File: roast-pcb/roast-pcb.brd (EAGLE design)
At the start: 3 parts

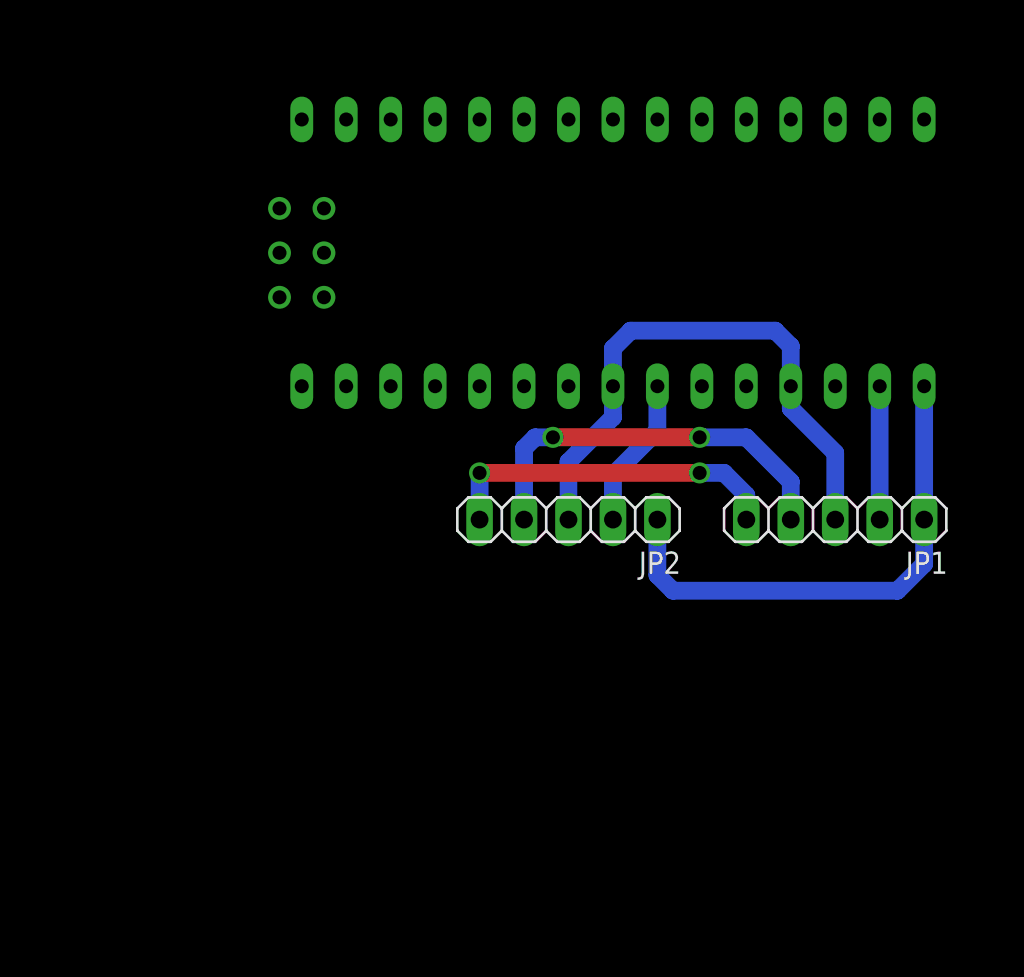
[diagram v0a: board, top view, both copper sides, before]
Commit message: ready to print PCB design
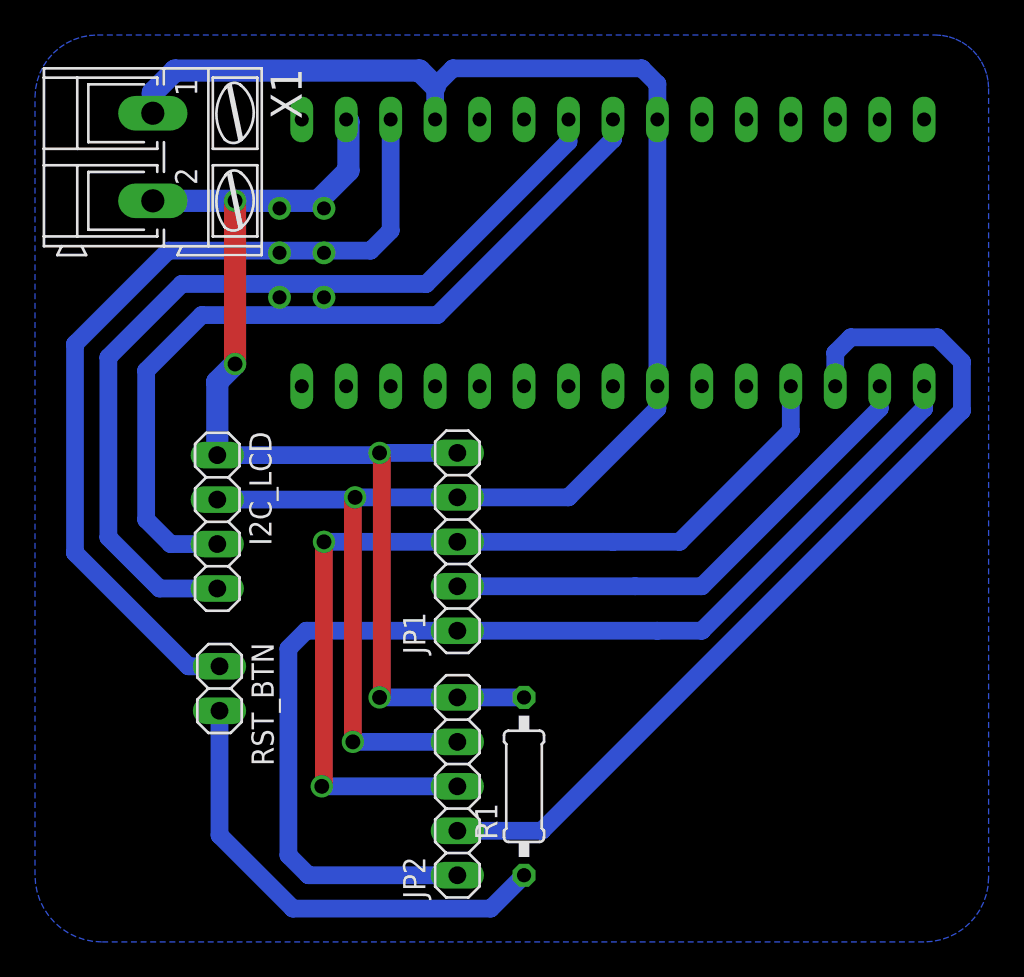
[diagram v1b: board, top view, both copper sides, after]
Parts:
- added I2C_LCD: (no value), pinhead:1X04
- added R1: (no value), rcl:0207/10
- added RST_BTN: (no value), pinhead:1X02
- added X1: (no value), con-ptr500:AK300/2
- moved JP1 21.6 mm to (38.1, 19.1), turned to 90 degrees
- moved JP2 16.5 mm to (38.1, 5.08), turned to 90 degrees
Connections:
- new net CS2: JP2.2, U$1.D10
- new net N$5: R1.1, RST_BTN.2
- new net SCL: I2C_LCD.4, U$1.A5
- new net SDA: I2C_LCD.3, U$1.A4
- net +5V: now also I2C_LCD.2, U$1.5V, X1.1
- net GND: now also I2C_LCD.1, R1.2, U$1.GND, X1.2
- net N$1: now also RST_BTN.1, U$1.RST; no longer JP2.2, U$1.D6
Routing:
- net +5V: track 22.8 -> 99.4 mm, vias 2 -> 4
- net CS2: track 0.00 -> 51.7 mm
- net SCL: track 0.00 -> 50.4 mm
- net SDA: track 0.00 -> 46.4 mm
- net GND: track 19.8 -> 65.7 mm, vias 2 -> 4
- net N$1: track 8.67 -> 49.9 mm
- net SO: track 29.6 -> 65.2 mm
- net N$5: track 0.00 -> 27.0 mm
- net CS1: track 7.62 -> 29.6 mm
- net SCK: track 32.7 -> 53.6 mm, vias 0 -> 4
- added copper zone on layer 16, net GND

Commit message: test ready sensor
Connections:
- new net N$4: U$1.RAW, X1.1
- net +5V: no longer X1.1
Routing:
- net +5V: track 99.4 -> 81.2 mm
- net N$4: track 0.00 -> 8.66 mm
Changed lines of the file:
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@@
 <wire x1="44.45" y1="21.59" x2="49.53" y2="26.67" width="1.016" layer="16"/>
 <wire x1="49.53" y1="26.67" x2="49.53" y2="45.212" width="1.016" layer="16"/>
-<contactref element="X1" pad="1"/>
-<wire x1="20.701" y1="43.5356" x2="20.701" y2="44.704" width="1.27" layer="16"/>
-<wire x1="20.701" y1="44.704" x2="21.971" y2="45.974" width="1.27" layer="16"/>
-<wire x1="21.971" y1="45.974" x2="35.941" y2="45.974" width="1.27" layer="16"/>
-<wire x1="35.941" y1="45.974" x2="36.83" y2="45.085" width="1.27" layer="16"/>
 </signal>
 <signal name="GND">
@@
 <wire x1="22.352" y1="33.782" x2="36.322" y2="33.782" width="1.016" layer="16"/>
 </signal>
+<signal name="N$4">
+<contactref element="X1" pad="1"/>
+<contactref element="U$1" pad="RAW"/>
+<wire x1="20.701" y1="43.5356" x2="25.0444" y2="43.5356" width="1.016" layer="16"/>
+<wire x1="25.0444" y1="43.5356" x2="25.4" y2="43.18" width="1.016" layer="16"/>
+<wire x1="25.4" y1="43.18" x2="29.21" y2="43.18" width="1.016" layer="16"/>
+</signal>
 </signals>
